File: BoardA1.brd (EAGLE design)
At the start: 44 x 93 mm, 18 parts, among them J2 FEMALE 2x3

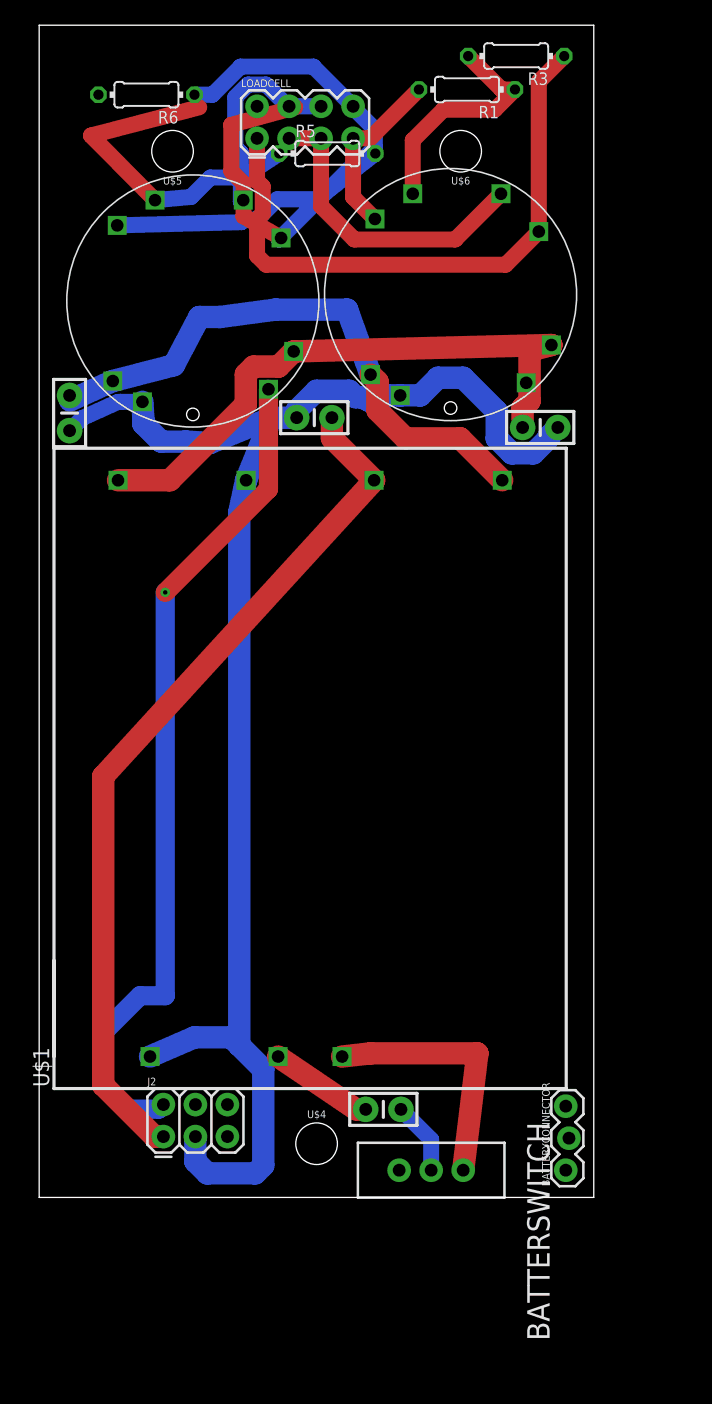
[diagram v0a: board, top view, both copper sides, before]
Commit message: Routing the power board
Work in progress
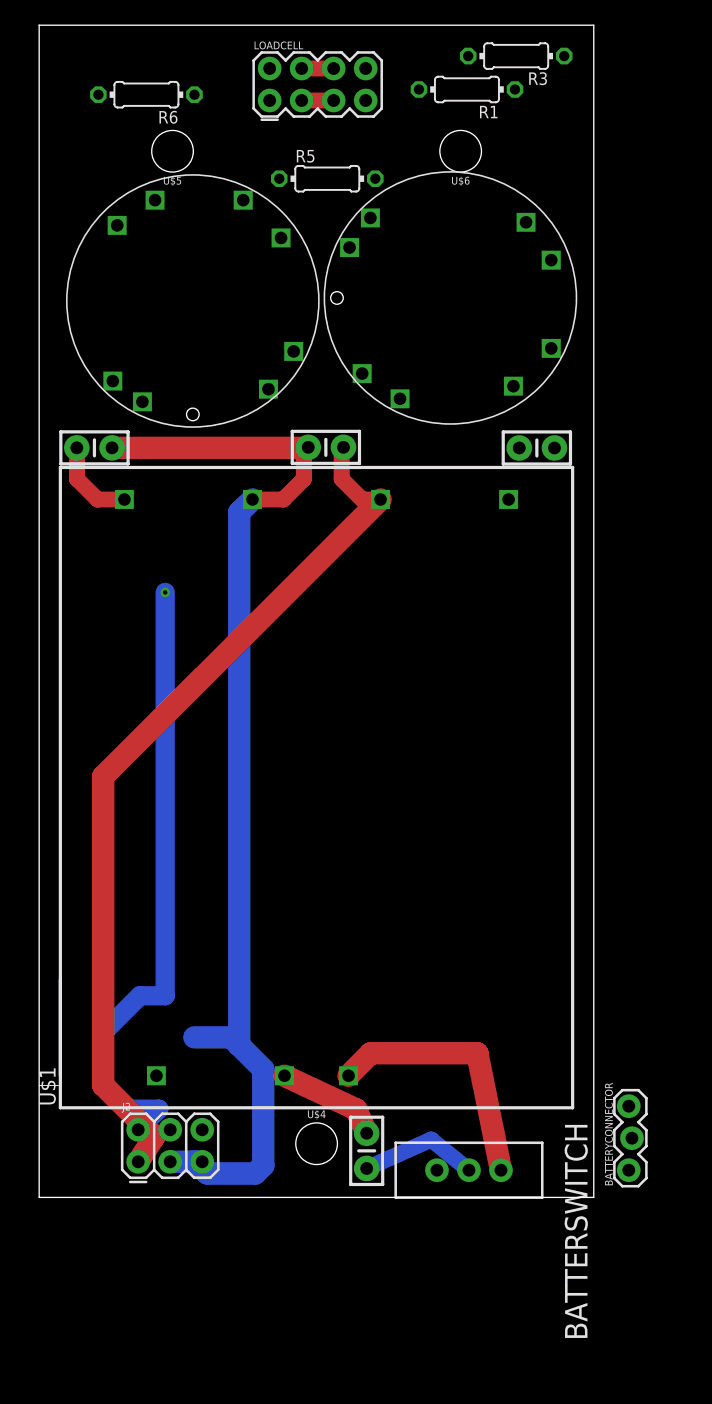
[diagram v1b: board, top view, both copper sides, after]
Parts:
- moved C2 37.2 mm to (39.5, 59.5), turned to 0 degrees
- moved C4 35.4 mm to (4.38, 59.5)
- moved BATTERYCONNECTOR 5.00 mm to (46.9, 2.16)
- moved C1 3.54 mm to (26.0, 3.69), turned to 270 degrees
- moved LOADCELL 3.16 mm to (22.1, 88.3)
- moved BATTERSWITCH 3.00 mm to (34.1, 2.16)
- moved J2 2.83 mm to (7.86, 2.83)
- moved C3 2.53 mm to (22.7, 59.5)
- moved R5 2.00 mm to (22.9, 80.8)
- moved U$1 1.61 mm to (11.8, 32.5)
- moved UPP_LC_AMP1 0.27 mm to (32.6, 71.4), turned to 180 degrees
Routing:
- net -EX1: track 48.2 -> 0.00 mm
- net -EX2: track 46.1 -> 0.00 mm
- net +15V: track 46.0 -> 0.00 mm
- net -15V: track 48.1 -> 6.91 mm
- net GND: track 125.1 -> 88.7 mm
- net +SIG2: track 27.2 -> 0.00 mm
- net +EX2: track 22.5 -> 0.00 mm
- net -SIG1: track 24.8 -> 2.54 mm
- net +SIG1: track 18.8 -> 0.00 mm
- net CH2: track 67.6 -> 49.9 mm
- net -SIG2: track 16.6 -> 2.54 mm
- net +EX1: track 13.9 -> 0.00 mm
- net N$1: track 5.82 -> 9.46 mm
- net 5V: track 69.2 -> 70.0 mm

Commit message: Rerouting 1
Please do not push now. Thanks
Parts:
- moved C1 8.52 mm to (17.5, 4.08)
- moved BATTERYCONNECTOR 4.11 mm to (43.3, 4.15), turned to 0 degrees
- moved BATTERSWITCH 2.75 mm to (31.8, 3.68)
- moved UPP_LC_AMP2 1.02 mm to (11.2, 71.1)
- moved UPP_LC_AMP1 0.36 mm to (32.9, 71.1)
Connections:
- new net DC-CTRL: J2.2, U$1.3
- new net N$4: BATTERSWITCH.2, BATTERYCONNECTOR.3
- net +EX2: now also LOADCELL.2
- net 5V: no longer J2.1
- net CH2: no longer J2.2
- net GND: now also J2.1; no longer J2.3, U$1.3
- net N$1: now also BATTERYCONNECTOR.1; no longer BATTERSWITCH.2
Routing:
- net 5V: track 70.0 -> 6.30 mm
- net CH2: track 49.9 -> 0.00 mm, vias 1 -> 0
- net -15V: track 6.91 -> 45.1 mm
- net +15V: track 0.00 -> 33.1 mm
- net GND: track 88.7 -> 110.6 mm
- net N$3: track 20.4 -> 0.00 mm
- net N$1: track 9.46 -> 0.00 mm
- net DC-CTRL: track 0.00 -> 5.77 mm
- net N$2: track 8.35 -> 5.00 mm

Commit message: Update 2
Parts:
- moved R5 19.5 mm to (3.48, 83.3), turned to 270 degrees
- moved R3 8.01 mm to (41.3, 83.3), flipped to the bottom, turned to 90 degrees
- moved BATTERYCONNECTOR 2.86 mm to (40.6, 5.08), turned to 270 degrees
- moved R6 2.29 mm to (10.8, 87.5)
- moved BATTERSWITCH 0.80 mm to (31.6, 4.45)
- moved R1 0.76 mm to (33.9, 88.7)
- moved UPP_LC_AMP1 0.76 mm to (32.9, 70.3), turned to 270 degrees
- moved UPP_LC_AMP2 0.38 mm to (11.2, 70.7)
- renumbered U$1 to DC_DC_CONVERTER
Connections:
- net 5V: now also J2.6
- net CH1: now also J2.5; no longer J2.4
- net CH2: now also J2.4
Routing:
- net CH1: track 0.00 -> 83.1 mm
- net -EX2: track 0.00 -> 64.5 mm
- net CH2: track 0.00 -> 61.3 mm
- net 5V: track 6.30 -> 66.2 mm, vias 0 -> 1
- net -SIG2: track 2.54 -> 55.6 mm
- net -EX1: track 0.00 -> 39.9 mm
- net +EX2: track 0.00 -> 29.4 mm
- net +15V: track 33.1 -> 55.7 mm
- net +SIG1: track 0.00 -> 20.5 mm
- net -SIG1: track 2.54 -> 20.9 mm
- net +EX1: track 0.00 -> 16.1 mm
- net N$3: track 0.00 -> 14.3 mm
- net +SIG2: track 0.00 -> 13.0 mm
- net GND: track 110.6 -> 123.5 mm
- net -15V: track 45.1 -> 55.5 mm
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
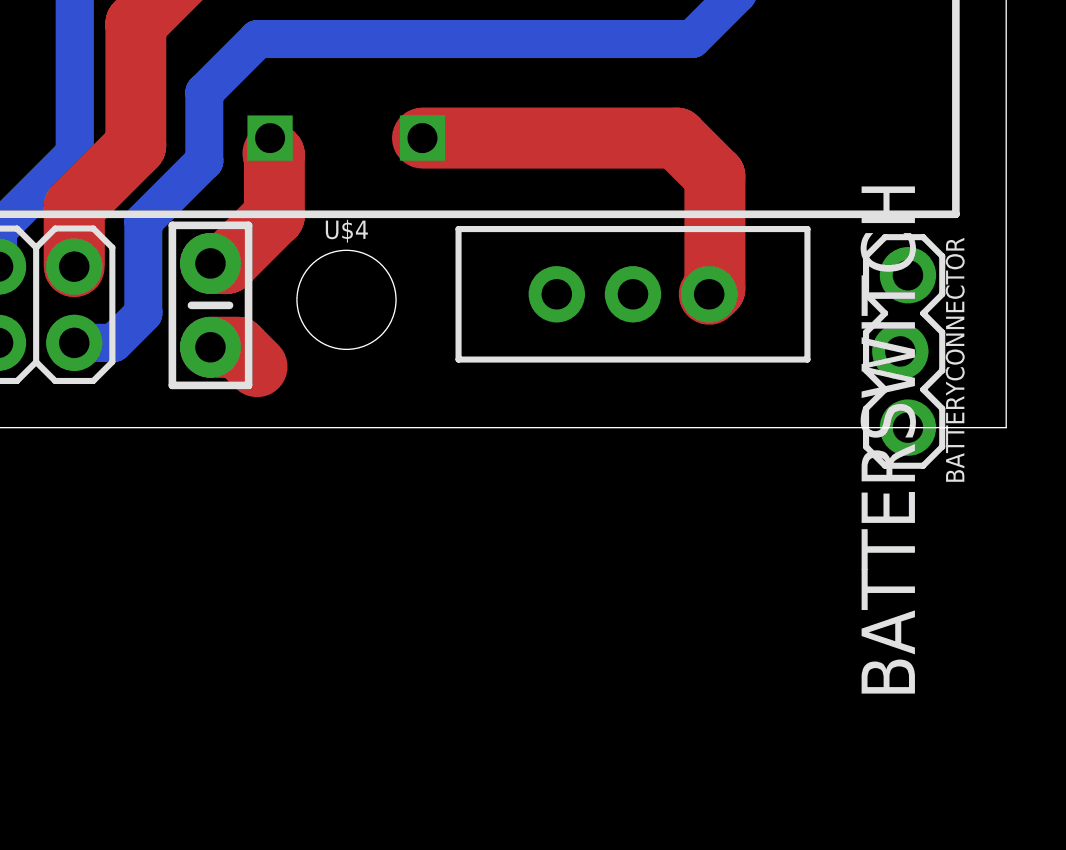
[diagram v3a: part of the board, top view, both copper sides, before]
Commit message: Changed Power connector
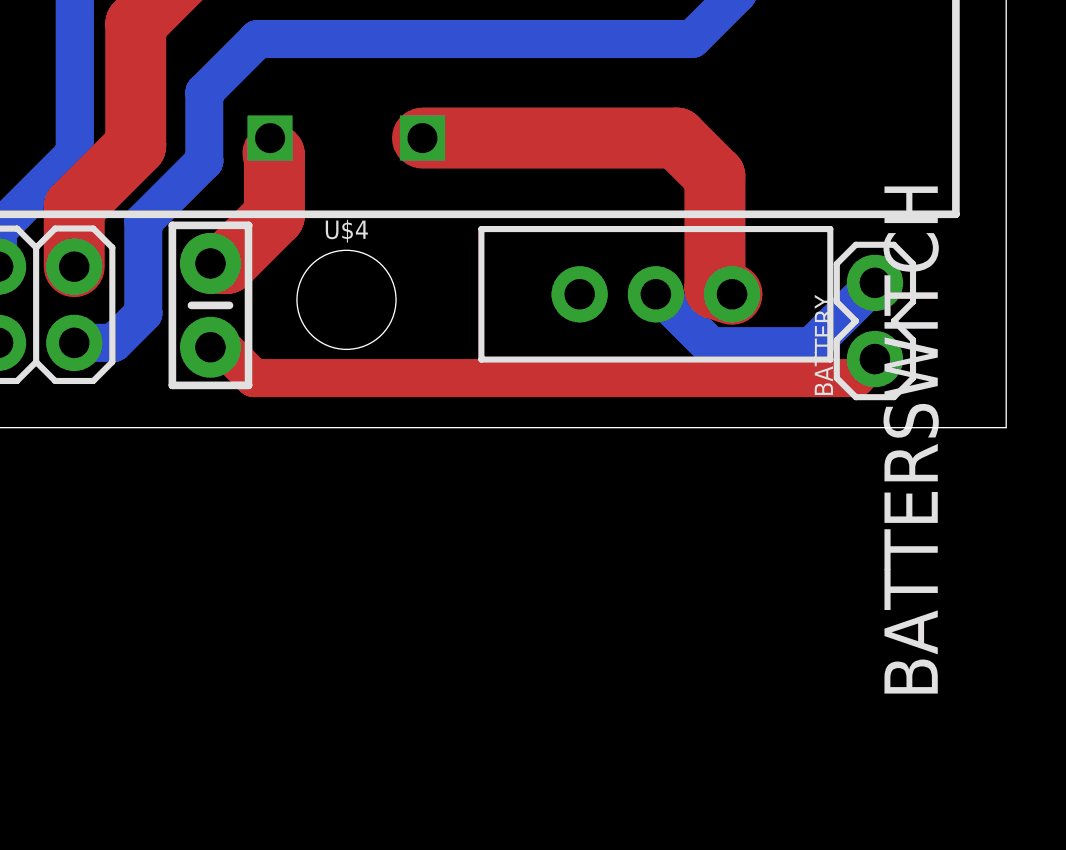
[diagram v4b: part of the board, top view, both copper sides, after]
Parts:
- removed BATTERYCONNECTOR: (no value), SparkFun-Connectors:1X03_LOCK
- added BATTERY: (no value), SparkFun-Connectors:1X02
- moved BATTERSWITCH 0.76 mm to (32.3, 4.45)
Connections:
- removed net N$4: BATTERSWITCH.2, BATTERYCONNECTOR.3
- new net N$5: BATTERSWITCH.2, BATTERY.2
- net N$1: now also BATTERY.1; no longer BATTERYCONNECTOR.1
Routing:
- net N$1: track 1.82 -> 22.8 mm
- net N$5: track 0.00 -> 8.89 mm
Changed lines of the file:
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@@
 <attribute name="SPICEPREFIX" value="R" x="10.796" y="87.487" size="1.778" layer="27" rot="R180" display="off"/>
 </element>
-<element name="BATTERSWITCH" library="SparkFun-Electromechanical" package="SWITCH-SPDT" value="" x="31.56" y="4.445" rot="R270">
-<attribute name="PROD_ID" value="SWCH-08261" x="31.56" y="4.445" size="1.778" layer="27" rot="R270" display="off"/>
+<element name="BATTERSWITCH" library="SparkFun-Electromechanical" package="SWITCH-SPDT" value="" x="32.322" y="4.445" rot="R270">
+<attribute name="PROD_ID" value="SWCH-08261" x="32.322" y="4.445" size="1.778" layer="27" rot="R270" display="off"/>
 </element>
 <element name="DC_DC_CONVERTER" library="Smartcrutches" package="DC-DCCONVERTER" value="" x="11.843" y="32.512" rot="R90"/>
@@
 <element name="U$6" library="SparkFun-Hardware" package="STAND-OFF" value="" x="33.44" y="83" rot="R180"/>
 <element name="LOADCELL" library="SparkFun-Connectors" package="2X4" value="" x="22.096" y="88.296"/>
-<element name="BATTERYCONNECTOR" library="SparkFun-Connectors" package="1X03_LOCK" value="" x="40.598" y="5.08" rot="R270"/>
+<element name="BATTERY" library="SparkFun-Connectors" package="1X02" value="" x="39.624" y="2.286" rot="R90"/>
 </elements>
 <signals>
@@
 <wire x1="33.02" y1="9.652" x2="34.29" y2="8.382" width="2.032" layer="1"/>
 <wire x1="34.29" y1="8.382" x2="34.29" y2="4.635" width="2.032" layer="1"/>
-<wire x1="34.29" y1="4.635" x2="34.1" y2="4.445" width="2.032" layer="1"/>
+<wire x1="34.29" y1="4.635" x2="34.862" y2="4.445" width="2.032" layer="1"/>
 </signal>
 <signal name="N$1">
 <contactref element="C1" pad="2"/>
-<contactref element="BATTERYCONNECTOR" pad="1"/>
-<wire x1="17.476" y1="2.679" x2="18.38245" y2="2.679" width="2.032" layer="1"/>
-<wire x1="18.38245" y1="2.679" x2="19.02945" y2="2.032" width="2.032" layer="1"/>
-<wire x1="19.02945" y1="2.032" x2="40.725" y2="5.08" width="0" layer="19" extent="1-1"/>
+<contactref element="BATTERY" pad="1"/>
+<wire x1="17.476" y1="2.679" x2="17.895" y2="2.679" width="1.27" layer="1"/>
+<wire x1="17.895" y1="2.679" x2="18.923" y2="1.651" width="1.27" layer="1"/>
+<wire x1="18.923" y1="1.651" x2="38.989" y2="1.651" width="1.27" layer="1"/>
+<wire x1="38.989" y1="1.651" x2="39.624" y2="2.286" width="1.27" layer="1"/>
 </signal>
 <signal name="GND">
@@
 <wire x1="7.62" y1="5.6012" x2="7.8552" y2="5.366" width="1.27" layer="1"/>
 </signal>
-<signal name="N$4">
+<signal name="N$5">
+<contactref element="BATTERY" pad="2"/>
 <contactref element="BATTERSWITCH" pad="2"/>
-<contactref element="BATTERYCONNECTOR" pad="3"/>
-<wire x1="31.56" y1="4.445" x2="40.725" y2="0" width="0" layer="19" extent="1-1"/>
+<wire x1="39.624" y1="4.826" x2="41.0718" y2="6.4262" width="0" layer="19" extent="1-16"/>
+<wire x1="32.322" y1="4.445" x2="32.41936875" y2="4.445" width="1.27" layer="16"/>
+<wire x1="32.41936875" y1="4.445" x2="34.14656875" y2="2.7178" width="1.27" layer="16"/>
+<wire x1="34.14656875" y1="2.7178" x2="37.5158" y2="2.7178" width="1.27" layer="16"/>
+<wire x1="37.5158" y1="2.7178" x2="39.624" y2="4.826" width="1.27" layer="16"/>
 </signal>
 </signals>
